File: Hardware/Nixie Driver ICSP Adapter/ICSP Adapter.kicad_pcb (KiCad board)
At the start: 2 copper layers, 22.9 x 31.8 mm, 5 parts

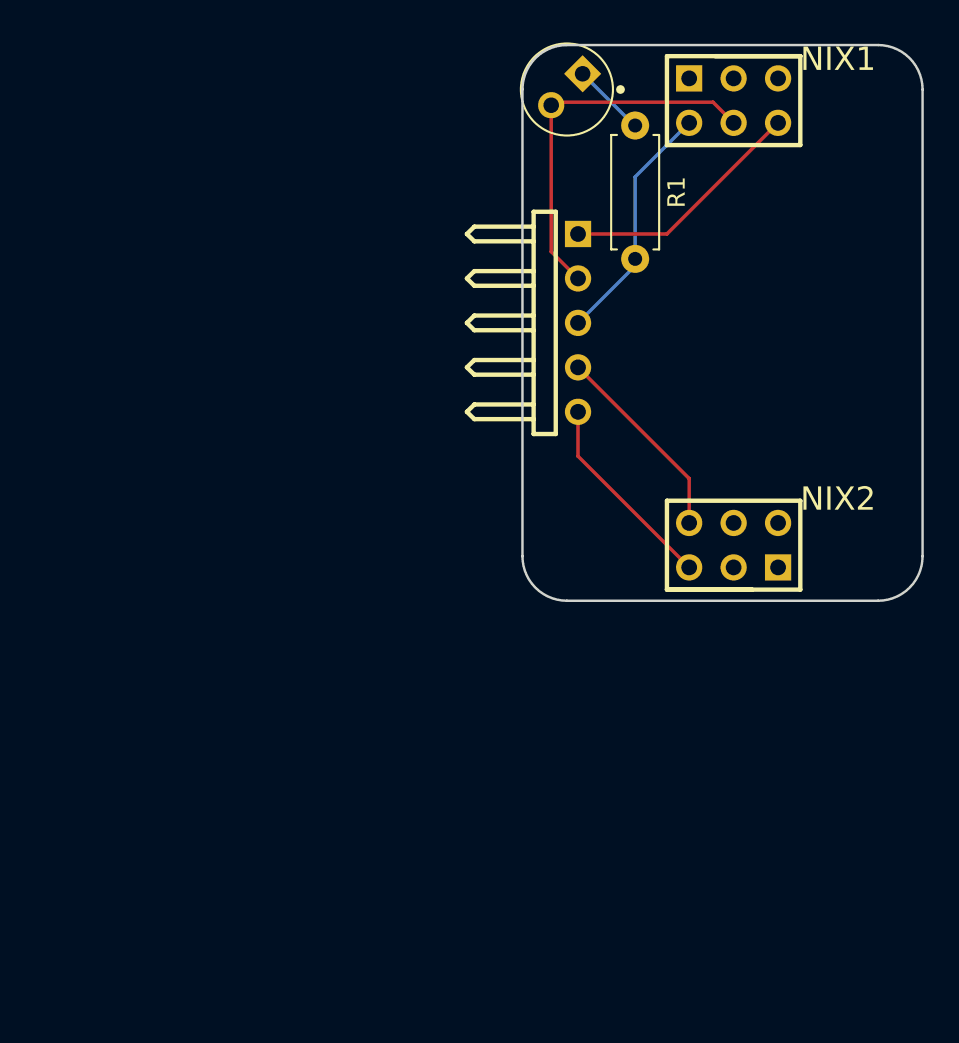
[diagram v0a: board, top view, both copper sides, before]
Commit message: Converted to native KiCad footprints and symbols
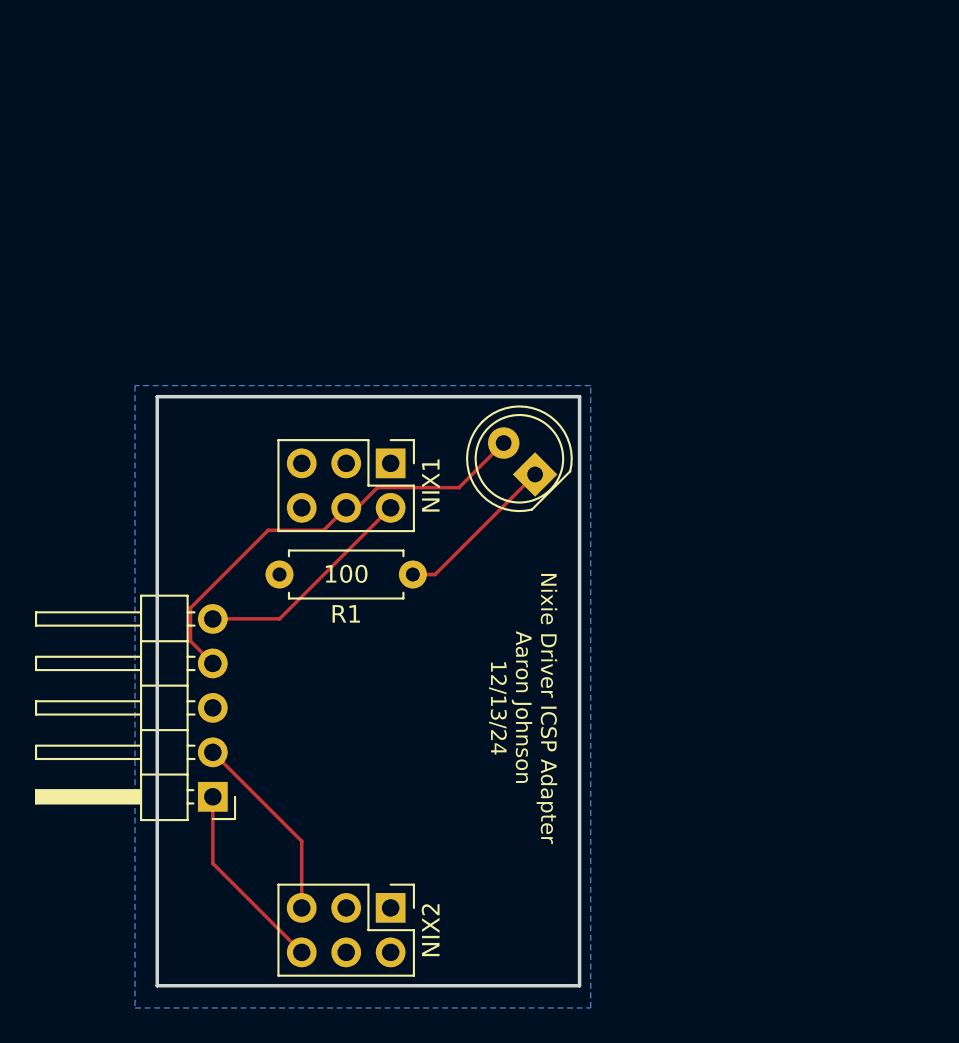
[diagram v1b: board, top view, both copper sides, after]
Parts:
- ICSP0: footprint ICSP Adapter:HDR-1x5H -> Connector_PinHeader_2.54mm:PinHeader_1x05_P2.54mm_Horizontal
- NIX1: footprint ICSP Adapter:HDRF-2x3 -> Connector_PinHeader_2.54mm:PinHeader_2x03_P2.54mm_Vertical
- NIX2: footprint ICSP Adapter:HDRF-2x3_NIX2 -> Connector_PinHeader_2.54mm:PinHeader_2x03_P2.54mm_Vertical
- PWR0: value LED-5MM ROUND GREEN -> LED-5MM_ROUND_GREEN; footprint ICSP Adapter:LED-5mm_Round_Green -> LED_THT:LED_D5.0mm
- moved ICSP0 34.2 mm to (119.4, 132.1), turned to 180 degrees
- moved R1 28.6 mm to (130.8, 119.4), turned to 180 degrees
- moved NIX2 28.5 mm to (129.5, 138.4), turned to -90 degrees
- moved NIX1 28.5 mm to (129.5, 113.0), turned to -90 degrees
- moved PWR0 22.1 mm to (137.8, 113.7), turned to 135.001 degrees
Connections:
- ICSP0 pad 1: ~{MCLR} -> SCLK
- ICSP0 pad 2: VDD -> SDAT
- ICSP0 pad 4: DAT -> VDD
- ICSP0 pad 5: CLK -> ~{MCLR}
- NIX1 pad 1: (no net) -> unconnected-(NIX1-P1-Pad1)
- NIX1 pad 2: GND -> ~{MCLR}
- NIX1 pad 3: (no net) -> unconnected-(NIX1-P3-Pad3)
- NIX1 pad 5: (no net) -> unconnected-(NIX1-P5-Pad5)
- NIX1 pad 6: ~{MCLR} -> GND
- NIX2 pad 1: (no net) -> unconnected-(NIX2-P1-Pad1)
- NIX2 pad 2: (no net) -> unconnected-(NIX2-P2-Pad2)
- NIX2 pad 3: (no net) -> unconnected-(NIX2-P3-Pad3)
- NIX2 pad 4: (no net) -> unconnected-(NIX2-P4-Pad4)
- NIX2 pad 5: CLK -> SDAT
- NIX2 pad 6: DAT -> SCLK
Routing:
- net GND: track 14.1 -> 0.00 mm
- net DAT: track 11.5 -> 0.00 mm
- net CLK: track 11.5 -> 0.00 mm
- net SDAT: track 0.00 -> 11.0 mm
- net SCLK: track 0.00 -> 11.0 mm
- net LED: track 4.23 -> 9.35 mm
- net VDD: track 21.5 -> 25.5 mm
- net ~{MCLR}: track 14.1 -> 12.8 mm
- added copper zone on B.Cu, net GND
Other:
- board size 22.9 x 31.8 mm -> 24.1 x 33.7 mm
- board text added: "Nixie Driver ICSP Adapter Aaron Johnson 12/13/24"
- board text added: "~{MCLR}"
- board text removed: "NIX1"
- board text removed: "NIX2"
- board text removed: "Nixie Driver ICSP Adapter 1/28/24"
- board text removed: "~MCLR"

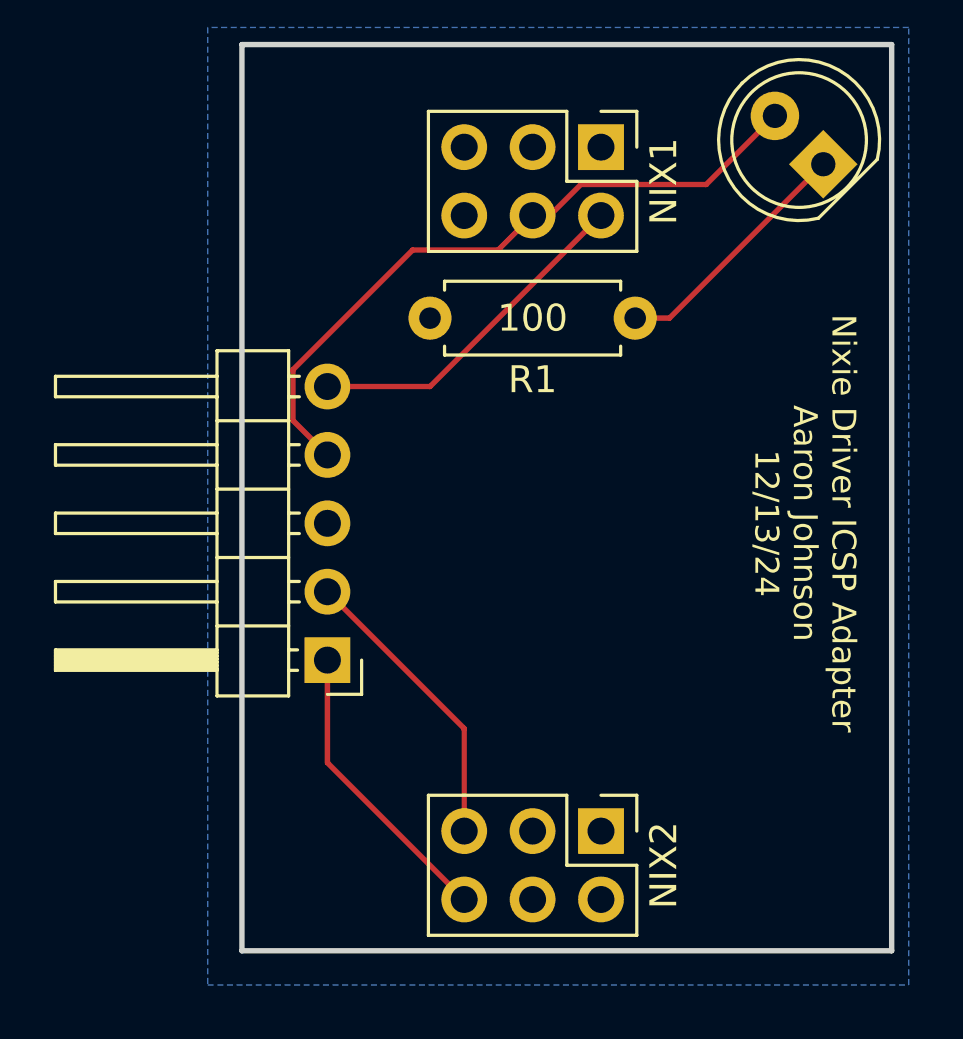
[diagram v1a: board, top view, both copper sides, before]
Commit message: Modified ICSP header footprint
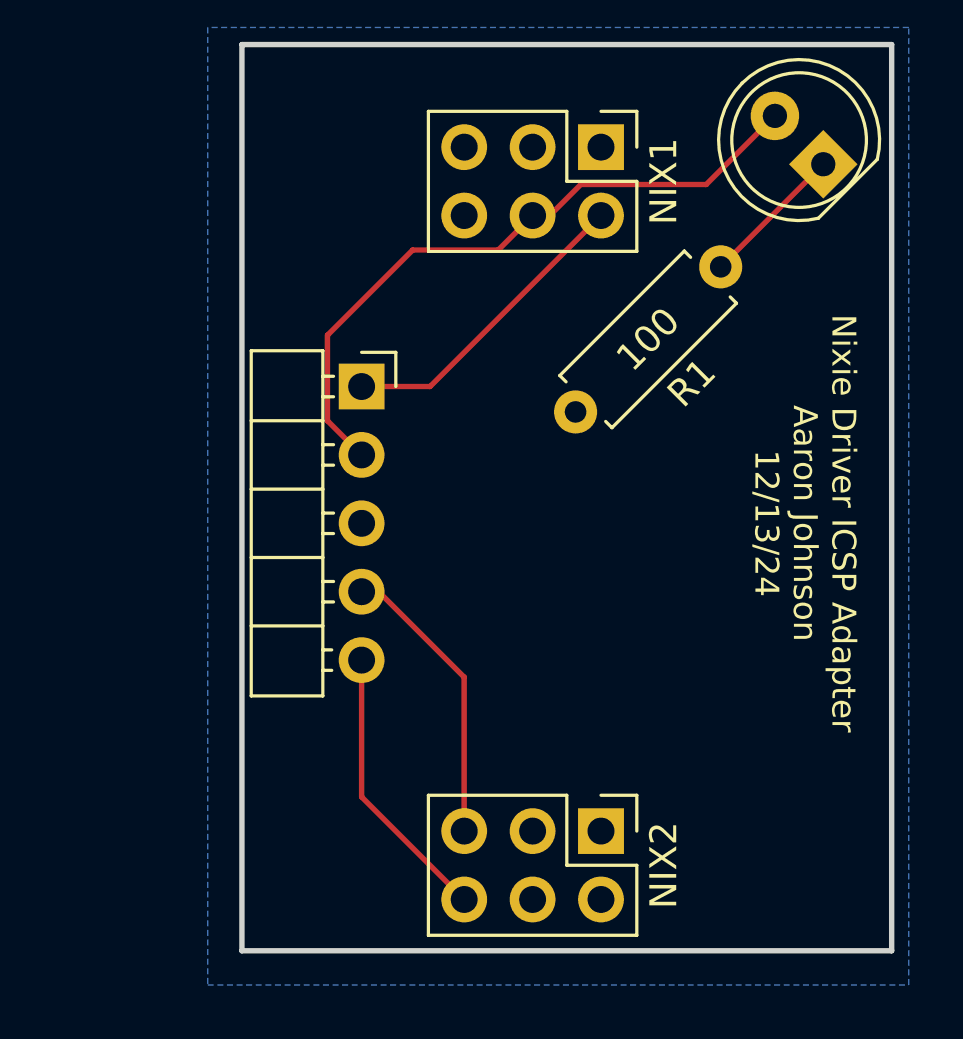
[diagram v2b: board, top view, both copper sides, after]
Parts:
- moved R1 3.70 mm to (134.0, 117.5), turned to -135 degrees
- moved ICSP0 1.27 mm to (120.7, 132.1)
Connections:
- ICSP0 pad 1: SCLK -> ~{MCLR}
- ICSP0 pad 2: SDAT -> VDD
- ICSP0 pad 4: VDD -> SDAT
- ICSP0 pad 5: ~{MCLR} -> SCLK
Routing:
- net LED: track 9.35 -> 5.39 mm
- net ~{MCLR}: track 12.8 -> 11.5 mm
- net VDD: track 25.5 -> 25.0 mm
- net SCLK: track 11.0 -> 10.5 mm
